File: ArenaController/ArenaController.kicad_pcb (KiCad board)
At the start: 2 copper layers, 80 x 90 mm, 30 parts, among them J1 RJ45, J2 RJ45, J4 RJ45, J5 RJ45, J6 RJ45, J8 Screw_Terminal_01x04, J9 Barrel_Jack_MountingPin, Q1 FS3400, Q2 FS3400, Q3 FS3400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

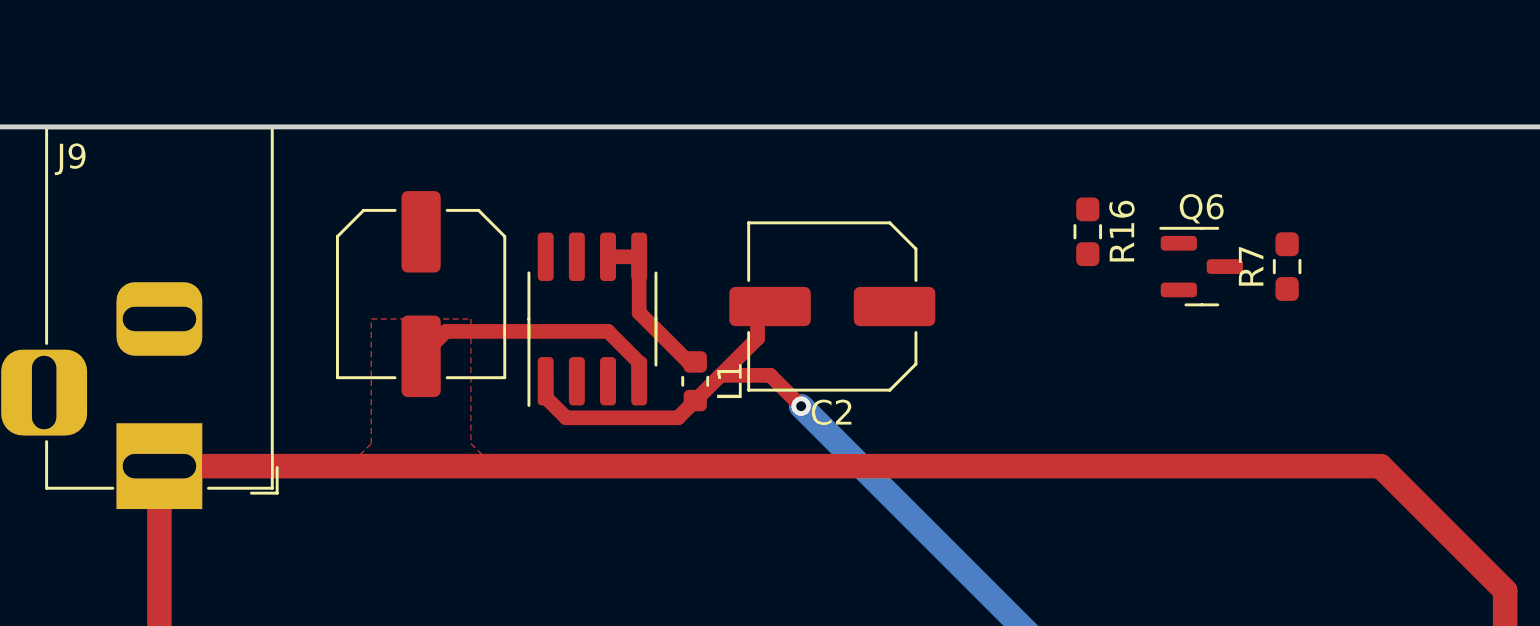
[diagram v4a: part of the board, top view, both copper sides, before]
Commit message: Work day fixes for schematic, including re-polarizing the caps.
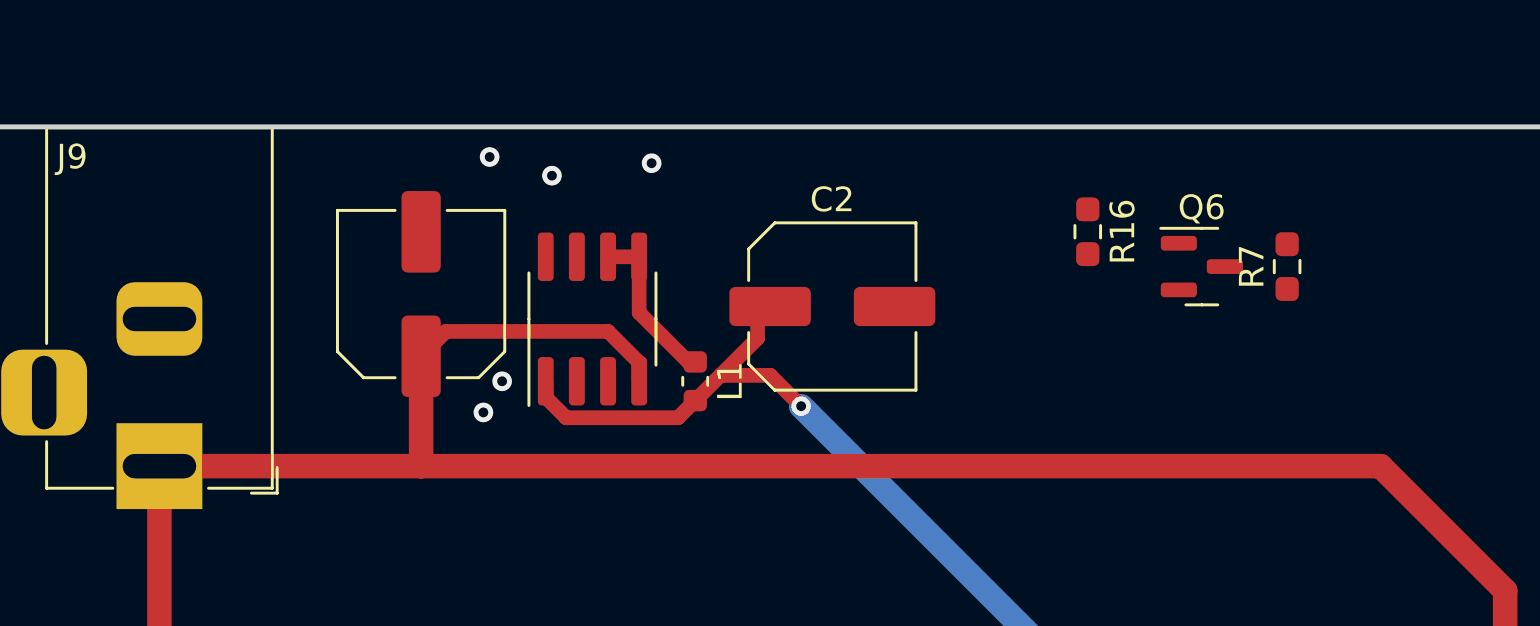
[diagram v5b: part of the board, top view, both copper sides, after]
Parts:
- C2: footprint Capacitor_SMD:C_Elec_6.3x7.7 -> Capacitor_SMD:C_Elec_6.3x5.4
- turned C1 to 90 degrees
- turned C2 to 0 degrees
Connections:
- C1 pad 1: GND -> +12V
- C1 pad 2: +12V -> GND
- C2 pad 1: GND -> +5V
- C2 pad 2: +5V -> GND
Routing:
- net +12V: track 107.6 -> 112.1 mm
- net GND: vias 22 -> 27
- removed copper zone on F.Cu, net +12V
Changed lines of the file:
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@@
     )
   )
-  (footprint "Capacitor_SMD:C_Elec_6.3x7.7" (layer "F.Cu")
-    (at 137.668 52.324 180)
-    (descr "SMD capacitor, aluminum electrolytic nonpolar, 6.3x7.7mm")
+  (footprint "Capacitor_SMD:C_Elec_6.3x5.4" (layer "F.Cu")
+    (at 137.668 52.324)
+    (descr "SMD capacitor, aluminum electrolytic nonpolar, 6.3x5.4mm")
     (tags "capacitor electrolyic nonpolar")
     (property "LCSC" "https://www.lcsc.com/product-detail/Aluminum-Electrolytic-Capacitors-SMD_ROQANG-RVT1C471M0607_C2977552.html")
     (property "Sheetfile" "ArenaController.kicad_sch")
     (property "Sheetname" "")
-    (property "ki_description" "Unpolarized capacitor")
+    (property "ki_description" "Polarized capacitor")
     (property "ki_keywords" "cap capacitor")
     (attr smd)
@@
     (fp_circle (center 0 0) (end 3.15 0)
       (stroke (width 0.1) (type solid)) (fill none) (layer "F.Fab"))
-    (pad "1" smd roundrect (at -2.5375 0 180) (size 3.325 1.6) (layers "F.Cu" "F.Paste" "F.Mask") (roundrect_rratio 0.15625)
-      (net 6 "GND") (pintype "passive"))
-    (pad "2" smd roundrect (at 2.5375 0 180) (size 3.325 1.6) (layers "F.Cu" "F.Paste" "F.Mask") (roundrect_rratio 0.15625)
+    (pad "1" smd roundrect (at -2.5375 0) (size 3.325 1.6) (layers "F.Cu" "F.Paste" "F.Mask") (roundrect_rratio 0.15625)
       (net 33 "+5V") (pintype "passive"))
-    (model "${KICAD6_3DMODEL_DIR}/Capacitor_SMD.3dshapes/C_Elec_6.3x7.7.wrl"
+    (pad "2" smd roundrect (at 2.5375 0) (size 3.325 1.6) (layers "F.Cu" "F.Paste" "F.Mask") (roundrect_rratio 0.15625)
+      (net 6 "GND") (pintype "passive"))
+    (model "${KICAD6_3DMODEL_DIR}/Capacitor_SMD.3dshapes/C_Elec_6.3x5.4.wrl"
       (offset (xyz 0 0 0))
       (scale (xyz 1 1 1))
@@
   )
   (footprint "Capacitor_SMD:C_Elec_6.3x5.4" (layer "F.Cu")
-    (at 120.904 51.816 -90)
+    (at 120.904 51.816 90)
     (descr "SMD capacitor, aluminum electrolytic nonpolar, 6.3x5.4mm")
     (tags "capacitor electrolyic nonpolar")
-    (property "LCSC" "https://www.lcsc.com/product-detail/Aluminum-Electrolytic-Capacitors-SMD_KNSCHA-RST100UF25V004_C4747964.html")
     (property "Sheetfile" "ArenaController.kicad_sch")
     (property "Sheetname" "")
-    (property "ki_description" "Unpolarized capacitor")
+    (property "ki_description" "Polarized capacitor")
     (property "ki_keywords" "cap capacitor")
     (attr smd)
@@
     (fp_circle (center 0 0) (end 3.15 0)
       (stroke (width 0.1) (type solid)) (fill none) (layer "F.Fab"))
-    (pad "1" smd roundrect (at -2.5375 0 270) (size 3.325 1.6) (layers "F.Cu" "F.Paste" "F.Mask") (roundrect_rratio 0.15625)
-      (net 6 "GND") (pintype "passive"))
-    (pad "2" smd roundrect (at 2.5375 0 270) (size 3.325 1.6) (layers "F.Cu" "F.Paste" "F.Mask") (roundrect_rratio 0.15625)
+    (pad "1" smd roundrect (at -2.5375 0 90) (size 3.325 1.6) (layers "F.Cu" "F.Paste" "F.Mask") (roundrect_rratio 0.15625)
       (net 1 "+12V") (pintype "passive"))
+    (pad "2" smd roundrect (at 2.5375 0 90) (size 3.325 1.6) (layers "F.Cu" "F.Paste" "F.Mask") (roundrect_rratio 0.15625)
+      (net 6 "GND") (pintype "passive"))
     (model "${KICAD6_3DMODEL_DIR}/Capacitor_SMD.3dshapes/C_Elec_6.3x5.4.wrl"
       (offset (xyz 0 0 0))
@@
   (segment (start 160.018825 58.832) (end 165.1 63.913175) (width 1) (layer "F.Cu") (net 1))
   (segment (start 129.794 54.61) (end 128.524 53.34) (width 0.6) (layer "F.Cu") (net 1))
-  (segment (start 110.236 58.832) (end 160.018825 58.832) (width 1) (layer "F.Cu") (net 1))
   (segment (start 163.351 84.045) (end 161 84.045) (width 1) (layer "F.Cu") (net 1))
   (segment (start 110.236 73.919) (end 109 75.155) (width 1) (layer "F.Cu") (net 1))
+  (segment (start 120.904 58.832) (end 160.018825 58.832) (width 1) (layer "F.Cu") (net 1))
   (segment (start 110.236 58.832) (end 110.236 73.919) (width 1) (layer "F.Cu") (net 1))
   (segment (start 129.794 55.372) (end 129.794 54.61) (width 0.6) (layer "F.Cu") (net 1))
+  (segment (start 120.904 58.832) (end 120.904 54.3535) (width 1) (layer "F.Cu") (net 1))
   (segment (start 128.524 53.34) (end 121.9175 53.34) (width 0.6) (layer "F.Cu") (net 1))
+  (segment (start 110.236 58.832) (end 120.904 58.832) (width 1) (layer "F.Cu") (net 1))
   (segment (start 165.1 82.296) (end 163.351 84.045) (width 1) (layer "F.Cu") (net 1))
   (segment (start 165.1 63.913175) (end 165.1 82.296) (width 1) (layer "F.Cu") (net 1))
@@
   (via (at 143.51 82.55) (size 0.8) (drill 0.4) (layers "F.Cu" "B.Cu") (free) (net 6))
   (via (at 134.112 100.076) (size 0.8) (drill 0.4) (layers "F.Cu" "B.Cu") (free) (net 6))
+  (via (at 123.444 56.642) (size 0.8) (drill 0.4) (layers "F.Cu" "B.Cu") (free) (net 6))
   (via (at 132.588 112.776) (size 0.8) (drill 0.4) (layers "F.Cu" "B.Cu") (free) (net 6))
   (via (at 163.322 71.374) (size 0.8) (drill 0.4) (layers "F.Cu" "B.Cu") (free) (net 6))
+  (via (at 130.302 46.482) (size 0.8) (drill 0.4) (layers "F.Cu" "B.Cu") (free) (net 6))
   (via (at 135.636 113.03) (size 0.8) (drill 0.4) (layers "F.Cu" "B.Cu") (free) (net 6))
   (via (at 164.338 109.728) (size 0.8) (drill 0.4) (layers "F.Cu" "B.Cu") (free) (net 6))
+  (via (at 126.238 46.99) (size 0.8) (drill 0.4) (layers "F.Cu" "B.Cu") (free) (net 6))
   (via (at 166.116 113.538) (size 0.8) (drill 0.4) (layers "F.Cu" "B.Cu") (free) (net 6))
   (via (at 156.21 83.058) (size 0.8) (drill 0.4) (layers "F.Cu" "B.Cu") (free) (net 6))
@@
   (via (at 152.908 93.472) (size 0.8) (drill 0.4) (layers "F.Cu" "B.Cu") (free) (net 6))
   (via (at 110.49 134.112) (size 0.8) (drill 0.4) (layers "F.Cu" "B.Cu") (free) (net 6))
+  (via (at 123.698 46.228) (size 0.8) (drill 0.4) (layers "F.Cu" "B.Cu") (free) (net 6))
   (via (at 115.062 108.458) (size 0.8) (drill 0.4) (layers "F.Cu" "B.Cu") (free) (net 6))
   (via (at 135.382 107.188) (size 0.8) (drill 0.4) (layers "F.Cu" "B.Cu") (free) (net 6))
+  (via (at 124.206 55.372) (size 0.8) (drill 0.4) (layers "F.Cu" "B.Cu") (free) (net 6))
   (via (at 156.464 72.136) (size 0.8) (drill 0.4) (layers "F.Cu" "B.Cu") (free) (net 6))
   (via (at 113.792 105.156) (size 0.8) (drill 0.4) (layers "F.Cu" "B.Cu") (free) (net 6))
@@
   (segment (start 129.794 50.297) (end 128.524 50.297) (width 0.6) (layer "F.Cu") (net 71))
   (segment (start 131.8005 54.5845) (end 129.794 52.578) (width 0.6) (layer "F.Cu") (net 71))
-  (zone (net 1) (net_name "+12V") (layer "F.Cu") (hatch edge 0.5)
-    (priority 2)
-    (connect_pads yes (clearance 0.508))
-    (min_thickness 0.25) (filled_areas_thickness no)
-    (fill yes (thermal_gap 0.5) (thermal_bridge_width 0.5))
-    (polygon
-      (pts
-        (xy 121.412 52.832)
-        (xy 122.936 52.832)
-        (xy 122.936 57.912)
-        (xy 123.952 58.928)
-        (xy 117.856 58.928)
-        (xy 118.872 57.912)
-        (xy 118.872 52.832)
-      )
-    )
-  )
   (zone (net 6) (net_name "GND") (layers "F&B.Cu") (hatch edge 0.5)
     (connect_pads (clearance 0.508))

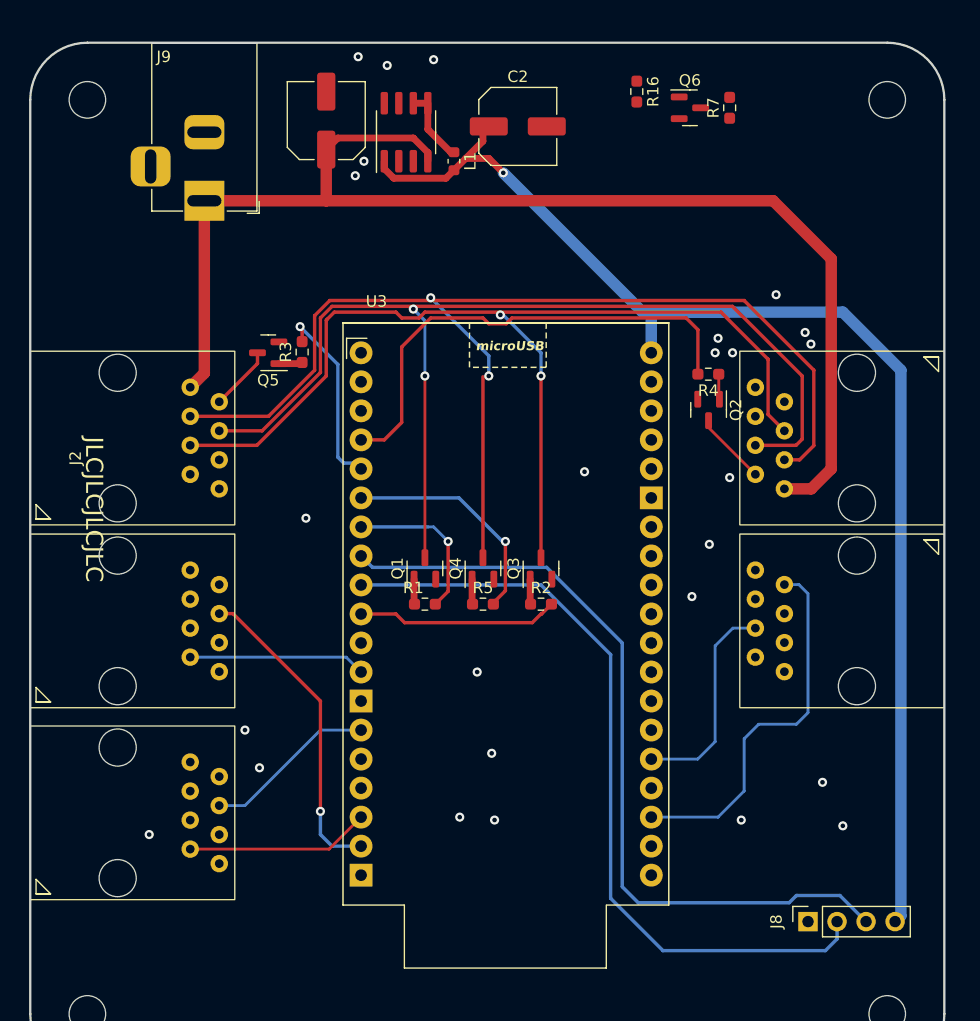
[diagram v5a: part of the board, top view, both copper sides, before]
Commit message: Update PCB errors and also remove software from this repo.
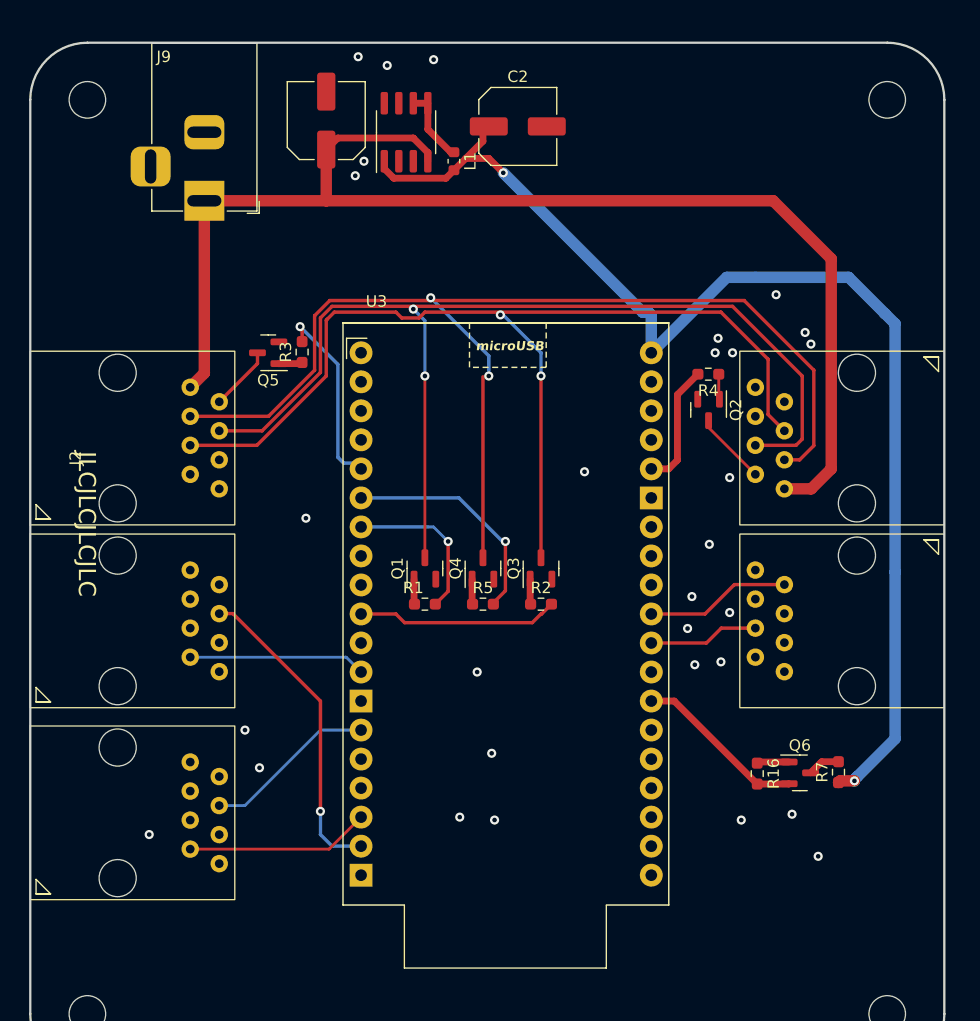
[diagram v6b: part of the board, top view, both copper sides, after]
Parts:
- removed J8: Screw_Terminal_01x04, Connector_PinSocket_2.54mm:PinSocket_1x04_P2.54mm_Vertical
- moved R16 60.6 mm to (158.6, 109.0)
- moved Q6 59.0 mm to (162.4, 108.9)
- moved R7 58.9 mm to (165.7, 108.8)
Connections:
- U3 pad 22: /T_A_End -> unconnected-(U3-RTC_GPIO0/SensVP/ADC1_0/GPIO36-Pad22)
- U3 pad 24: /T_A_Start -> unconnected-(U3-RTC_GPIO4/ADC1_6/GPIO34-Pad24)
- U3 pad 26: unconnected-(U3-RTC_GPIO9/XTal32P/Touch9/ADC1_4/GPIO32-Pad26) -> /status_LED
- U3 pad 28: unconnected-(U3-DAC_1/RTC_GPIO6/ADC2_8/GPIO25-Pad28) -> /T_A_Start
- U3 pad 29: unconnected-(U3-DAC_2/RTC_GPIO7/ADC2_9/GPIO26-Pad29) -> /T_A_End
- U3 pad 34: unconnected-(U3-RTC_GPIO14/Touch4/HSPI_ID/ADC2_4/GPIO13-Pad34) -> /m_Red_1
- U3 pad 4: /m_Red_1 -> unconnected-(U3-GPIO15/ADC2_3/HSPI_CS0/Touch3/RTC_GPIO13-Pad4)
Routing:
- net /Dis_serial_Rx: track 70.5 -> 0.00 mm
- net /Dis_Serial_Tx: track 69.4 -> 0.00 mm
- net /m_Red_1: track 42.5 -> 10.9 mm
- net /T_A_End: track 33.0 -> 12.7 mm
- net /status_LED: track 0.00 -> 15.1 mm
- net +5V: track 117.5 -> 105.7 mm, vias 1 -> 2
- net /T_A_Start: track 18.8 -> 9.65 mm
- net /ws2812b_output: track 0.00 -> 2.85 mm
- net +3.3V: track 0.00 -> 2.84 mm
- net /m_Red_2: track 16.6 -> 15.9 mm
- net /s_Red_1: track 6.40 -> 5.79 mm
- net GND: vias 27 -> 31
